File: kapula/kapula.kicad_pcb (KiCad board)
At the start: 4 copper layers, 50 x 59 mm, 156 parts, among them J1 Conn_02x10_Odd_Even, J12 U.FL, J13 U.FL, J3 U.FL, J4 Conn_ARM_JTAG_SWD_10, J5 U.FL, J9 U.FL, Q1 AO3401A, Q2 AO3401A, Q3 AO3400A, Q4 BSS84, Q5 AO3400A, Q6 AO3400A, T1 BW21S7511A01TF, T2 BW21S7511A01TF, T3 BW21S7511A01TF, T4 BW21S7511A01TF, U1 XC6206P332MR, U2 TP4054, U3 DW01+G, U5 EFR32FG14P233F256GM48-B, U6 XA213-G4J, X1 DSB221SDN, Y1 32768 Hz

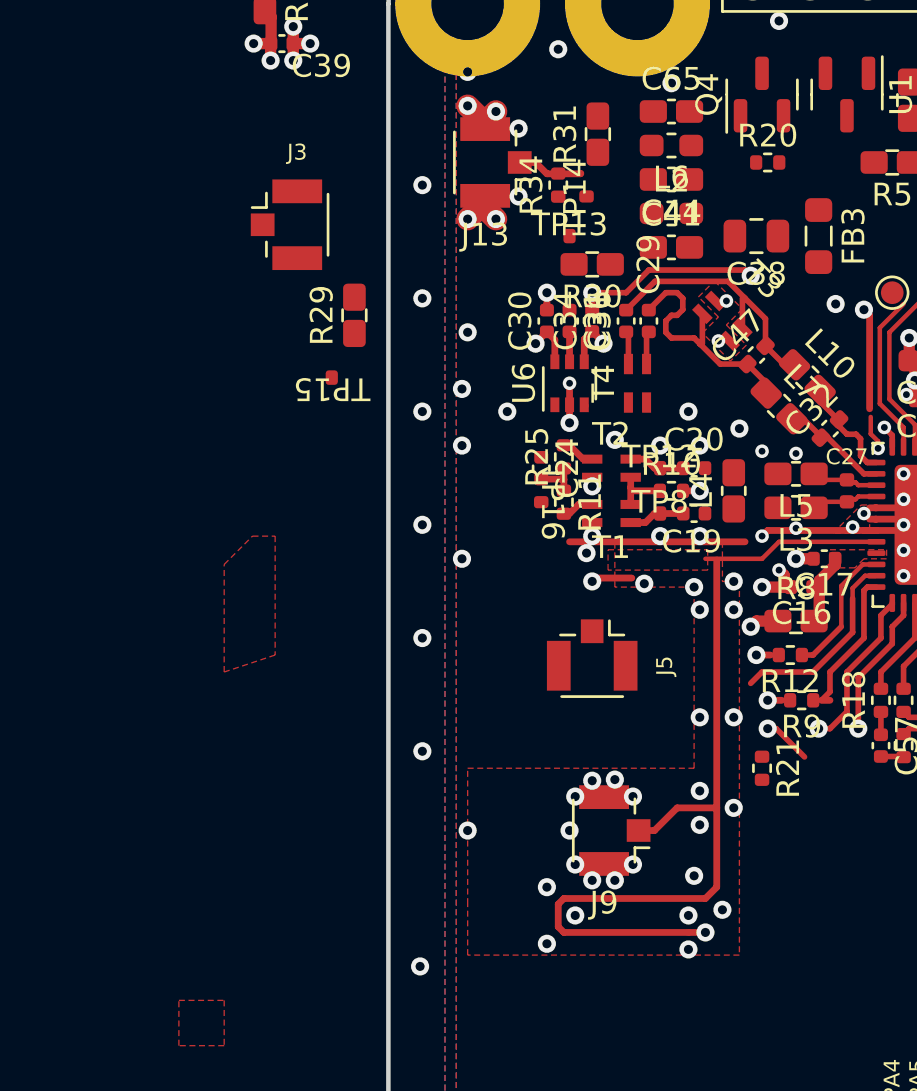
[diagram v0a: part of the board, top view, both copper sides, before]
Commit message: PCB: Organize RF layout
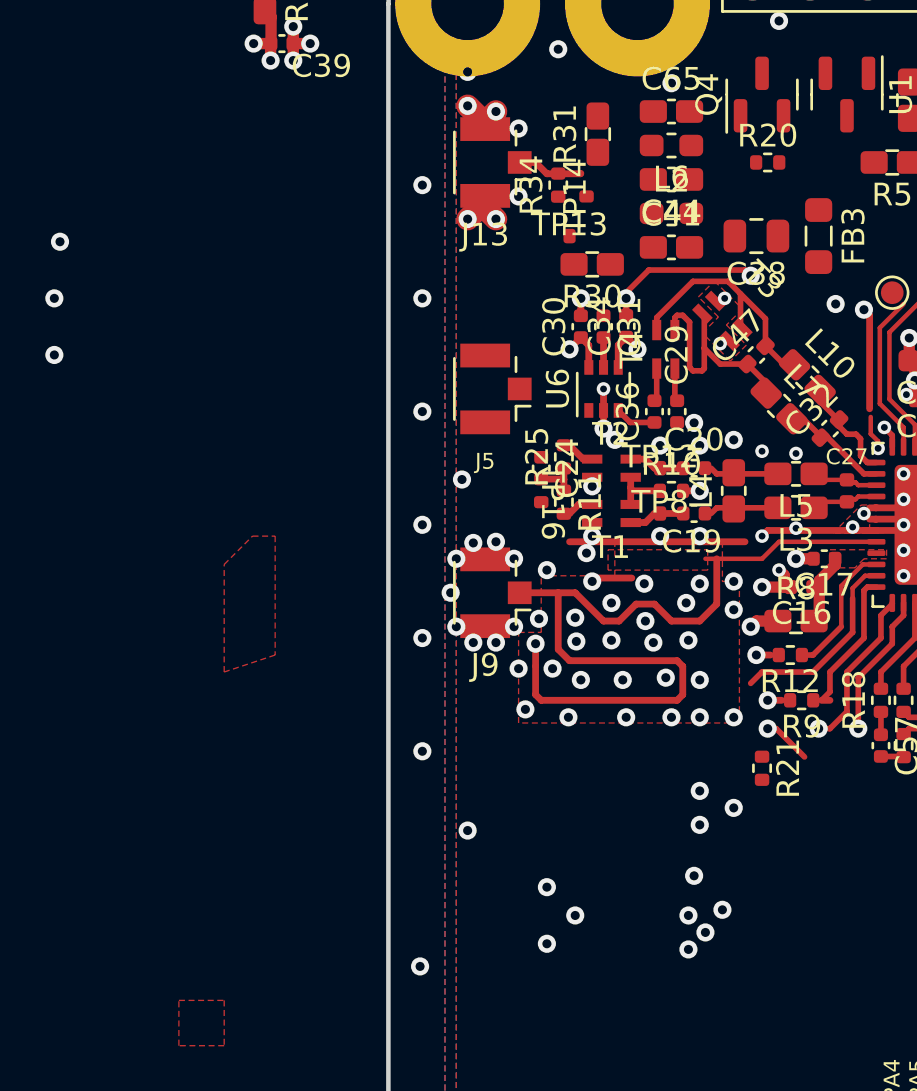
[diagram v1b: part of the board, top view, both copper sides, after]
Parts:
- removed J3: U.FL, Connector_Coaxial:U.FL_Hirose_U.FL-R-SMT-1_Vertical
- removed R29: 0, kapula:R_0402_to_0603_HandSolder
- removed TP15: ~, kapula:Pad_0402_1005Metric
- moved NT1 14.2 mm to (106.5, 89.8), turned to 90 degrees
- moved J5 12.5 mm to (104.8, 78.0), turned to 180 degrees
- moved J9 11.7 mm to (104.8, 87.0)
- moved C29 4.19 mm to (112.8, 79.0)
- moved C36 4.19 mm to (111.8, 79.0)
- moved T4 1.95 mm to (112.2, 76.2)
- moved C30 1.52 mm to (108.5, 75.2)
- moved C31 1.52 mm to (109.5, 75.2)
- moved C34 1.52 mm to (110.5, 75.2)
- moved U6 1.52 mm to (109.5, 78.0)
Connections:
- C29 pad 1: Net-(C29-Pad1) -> GND
- C36 pad 1: Net-(C36-Pad1) -> /RFSW_TX
- C47 pad 1: Net-(C29-Pad2) -> Net-(C47-Pad1)
- C47 pad 2: Net-(C36-Pad2) -> Net-(C47-Pad2)
- L10 pad 1: Net-(C36-Pad2) -> Net-(C47-Pad2)
- L7 pad 1: Net-(C29-Pad2) -> Net-(C47-Pad1)
- T3 pad 2: Net-(C36-Pad2) -> Net-(C47-Pad2)
- T3 pad 4: Net-(C29-Pad2) -> Net-(C47-Pad1)
- T4 pad 1: /RF_TX -> Net-(C36-Pad2)
- T4 pad 2: Net-(C36-Pad1) -> Net-(C47-Pad2)
- T4 pad 3: Net-(C29-Pad1) -> Net-(C47-Pad1)
- T4 pad 4: GND -> Net-(C29-Pad2)
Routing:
- net /TX_EN_SW: track 27.2 -> 3.86 mm
- net /RX_EN_SW: track 23.1 -> 2.82 mm, vias 3 -> 2
- net Net-(C47-Pad2): track 0.00 -> 11.4 mm
- net Net-(C47-Pad1): track 0.00 -> 10.7 mm
- net Net-(C36-Pad2): track 11.6 -> 1.46 mm
- net Net-(C29-Pad2): track 11.1 -> 1.46 mm
- net GND: track 91.1 -> 94.5 mm, vias 170 -> 190
- net Net-(C20-Pad2): track 0.00 -> 3.05 mm
- net Net-(C19-Pad2): track 0.00 -> 3.05 mm
- net /RF_2G4: track 40.1 -> 37.3 mm
- net /RFSW_TX: track 0.07 -> 1.89 mm
- net Net-(C36-Pad1): track 1.46 -> 0.00 mm
- net Net-(C29-Pad1): track 1.46 -> 0.00 mm

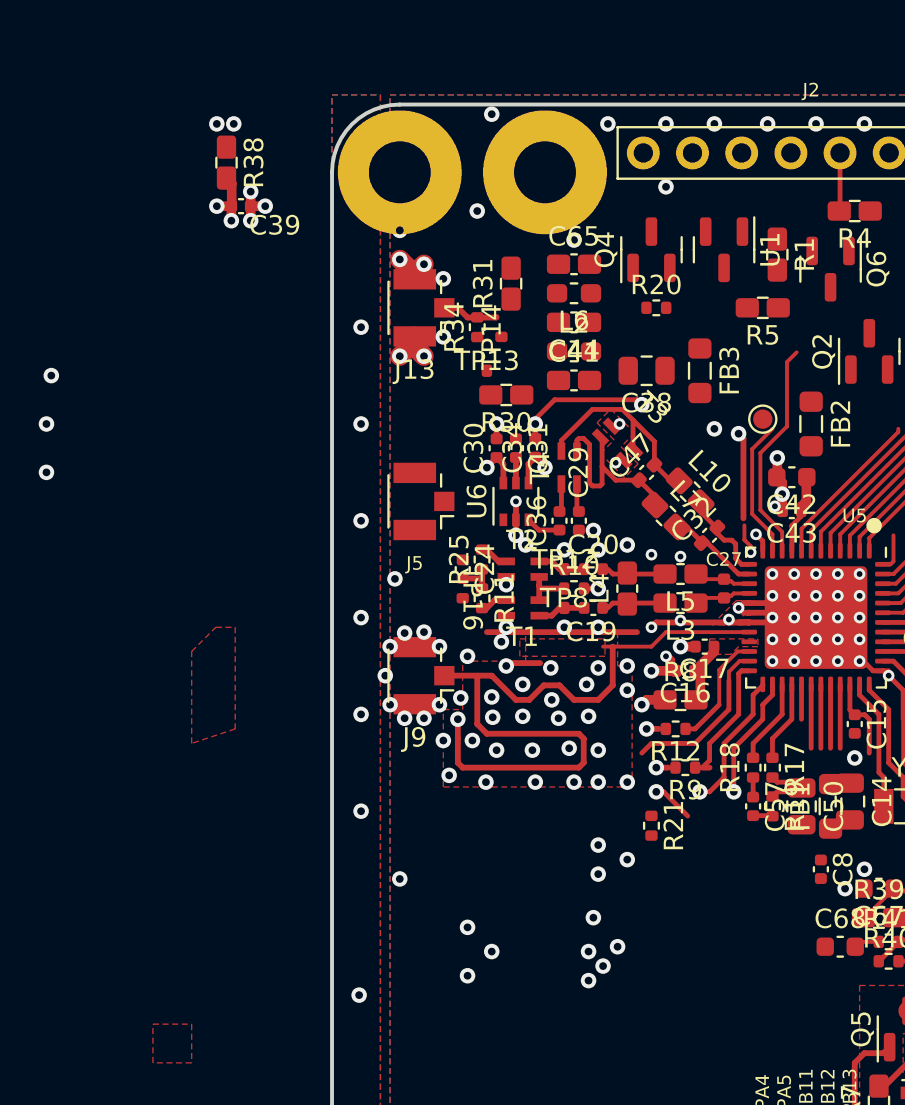
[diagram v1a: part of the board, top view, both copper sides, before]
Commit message: PCB: Layout more RF circuits
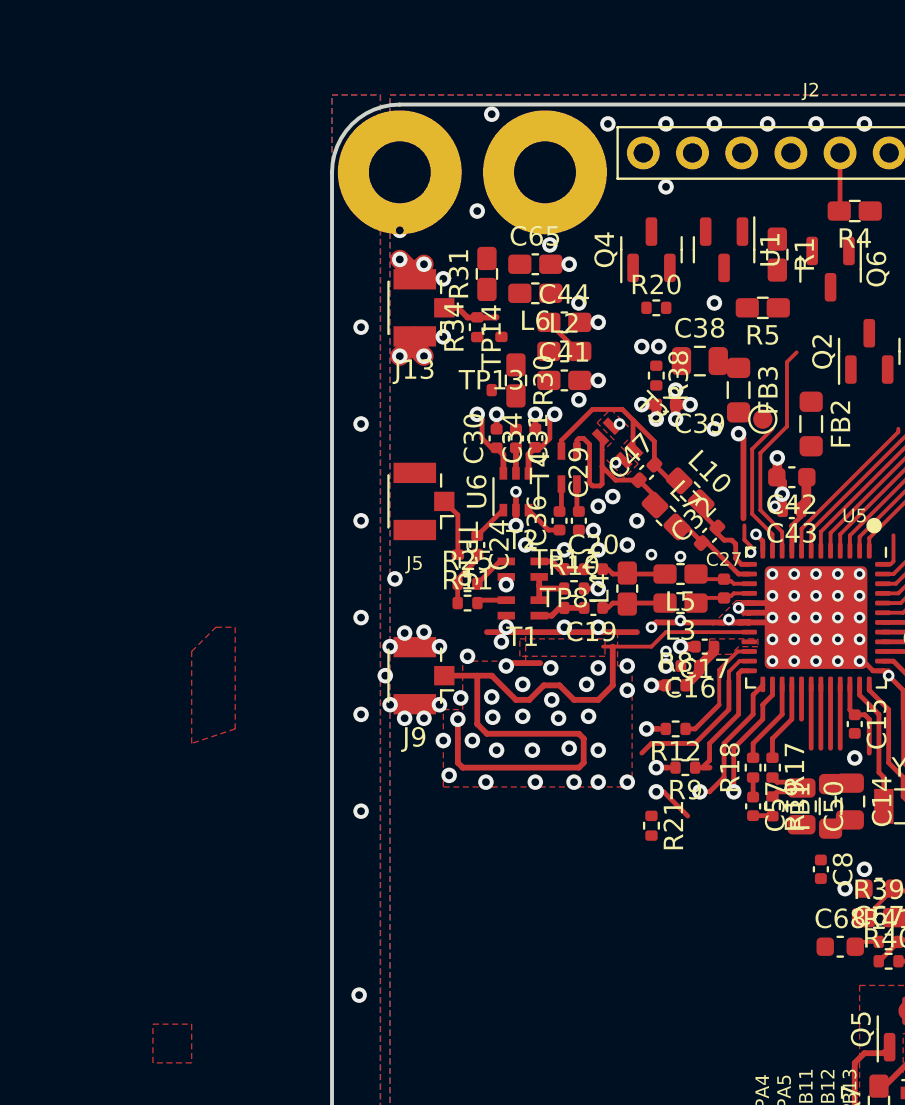
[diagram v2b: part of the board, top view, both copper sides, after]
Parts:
- C16: value 15p -> 220n
- C17: value 220n -> 15p
- L2, L6: value 18n -> 22n; footprint Inductor_SMD:L_0603_1608Metric_Pad1.05x0.95mm_HandSolder -> kapula:L_0402_to_0603_HandSolder
- R38, R8: footprint kapula:R_0402_to_0603_HandSolder -> Resistor_SMD:R_0402_1005Metric
- moved R38 24.8 mm to (116.8, 71.5)
- moved C39 24.2 mm to (117.2, 73.0)
- moved C38 2.80 mm to (119.0, 70.8), turned to 0 degrees
- moved TP16 2.26 mm to (106.5, 80.8)
- moved FB3 2.24 mm to (121.0, 72.2)
- moved C65 2.00 mm to (110.5, 65.8)
- moved L6 2.00 mm to (110.5, 67.2)
- moved C24 1.46 mm to (107.5, 80.2)
- moved R25 1.46 mm to (107.0, 82.2), turned to 0 degrees
- moved R31 1.35 mm to (108.0, 66.2)
- moved TP13 1.03 mm to (108.2, 72.2)
- moved R30 0.90 mm to (109.5, 71.8), turned to -90 degrees
- moved R11 0.79 mm to (107.0, 83.2), turned to 0 degrees
- moved R8 0.79 mm to (117.8, 87.5)
- moved C30 0.50 mm to (108.5, 74.8)
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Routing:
- net GND: track 94.5 -> 86.7 mm, vias 190 -> 183
- net /RFP_RX: track 0.00 -> 3.04 mm
- net Net-(C44-Pad1): track 0.00 -> 2.22 mm
- net /RFSW_RX: track 0.00 -> 1.90 mm
- net /RX_EN_SW: track 2.82 -> 4.39 mm
- net /PAVDD_SubG: track 3.09 -> 1.53 mm
- net /TX_EN_SW: track 3.86 -> 5.40 mm
- net /RF_RX: track 1.99 -> 2.68 mm
- added copper zone on F.Cu, net /PAVDD_2G4
- removed copper zone on F.Cu, net /PAVDD

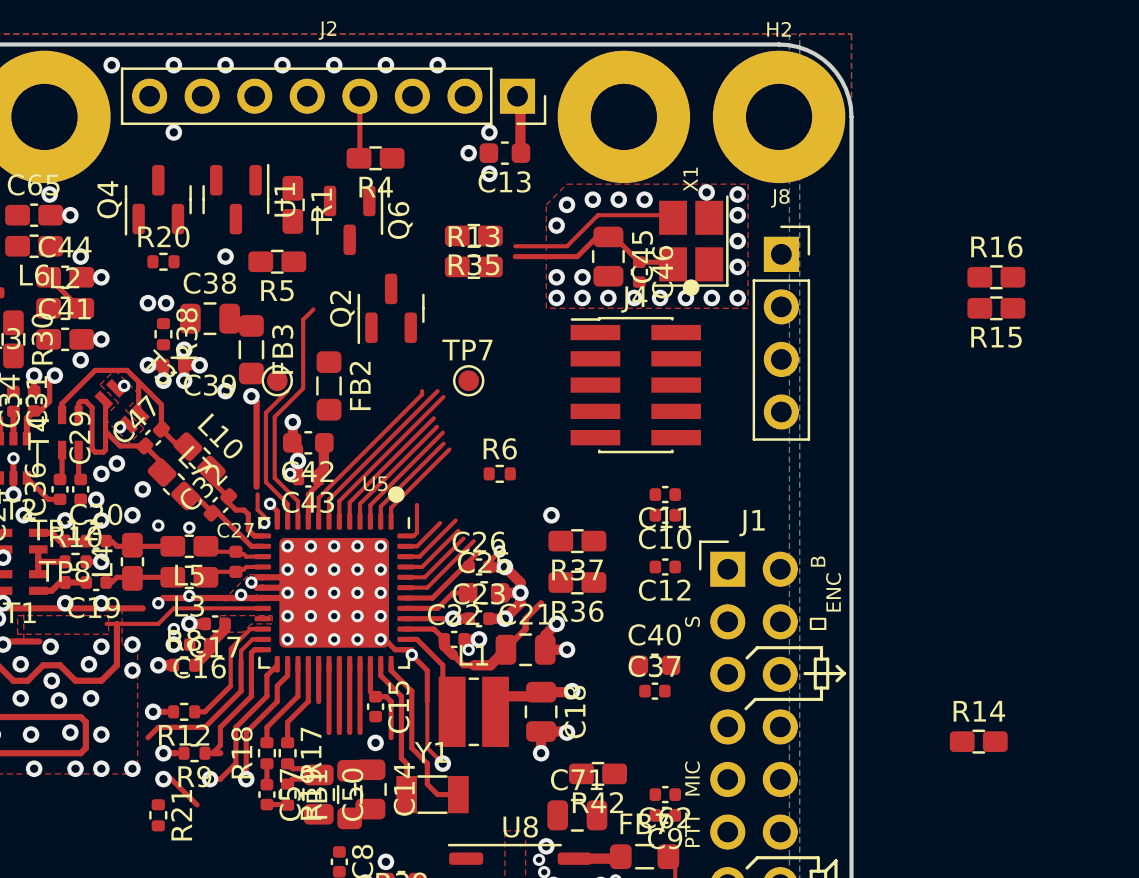
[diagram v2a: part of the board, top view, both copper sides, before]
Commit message: PCB: Route some display and connector lines
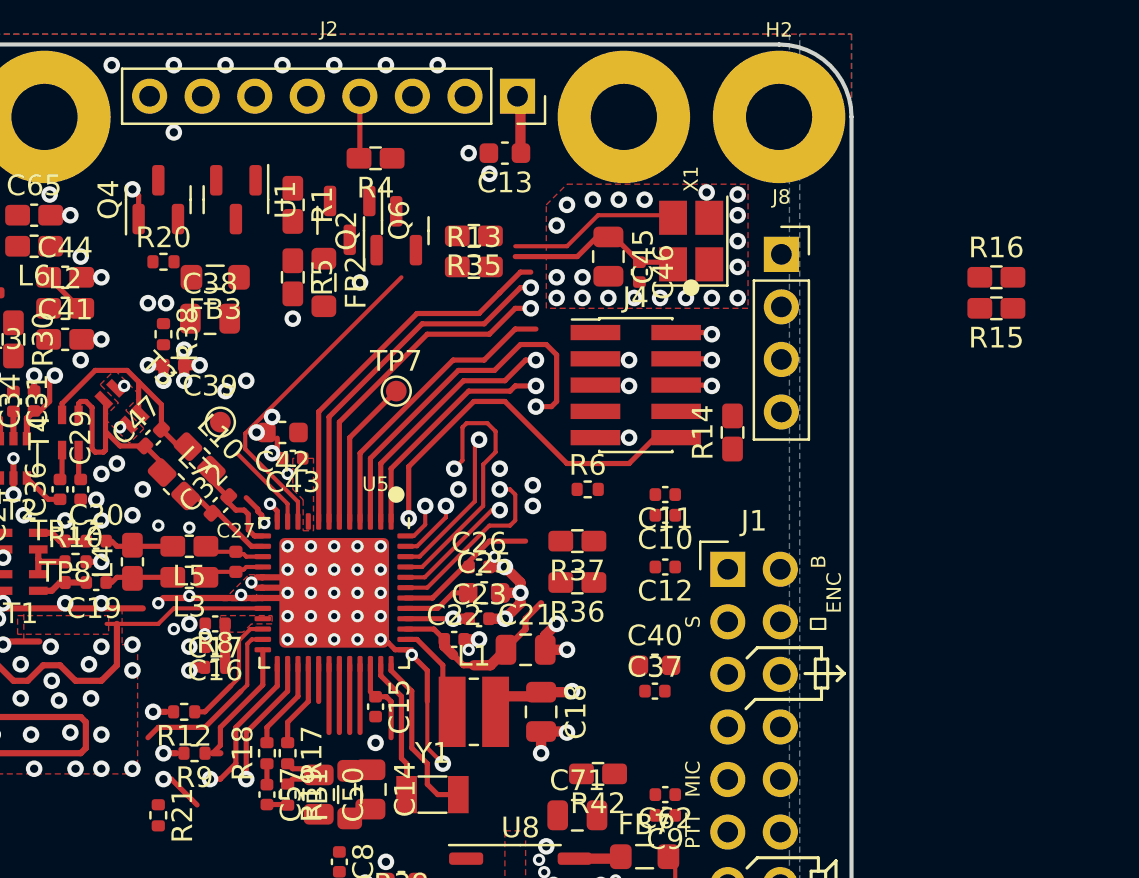
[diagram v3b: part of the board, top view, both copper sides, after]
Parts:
- moved R14 19.1 mm to (144.2, 76.2), turned to 90 degrees
- moved FB2 5.01 mm to (124.5, 69.0)
- moved R6 4.32 mm to (137.2, 79.0)
- moved FB3 3.91 mm to (119.2, 68.8), turned to 180 degrees
- moved Q2 3.76 mm to (128.0, 66.5)
- moved TP7 3.54 mm to (128.0, 74.2)
- moved TP11 3.40 mm to (119.5, 75.8)
- moved R8 1.50 mm to (119.2, 87.6)
- moved C42 1.35 mm to (122.5, 76.2)
- moved C43 1.25 mm to (123.0, 77.5)
- moved R5 1.06 mm to (123.0, 68.8), turned to -90 degrees
- moved C16 0.76 mm to (119.2, 86.6)
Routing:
- net /~{D_LED_EN}: track 2.14 -> 34.2 mm, vias 0 -> 2
- net /SWDIO_TMS: track 5.02 -> 28.8 mm, vias 0 -> 2
- net /SWO_TDO: track 5.75 -> 28.5 mm, vias 0 -> 2
- net /SWCLK_TCK: track 4.65 -> 27.0 mm, vias 0 -> 2
- net /D_CS: track 8.03 -> 28.8 mm, vias 0 -> 1
- net /RESET: track 5.97 -> 26.5 mm, vias 1 -> 2
- net /~{VDDS_EN}: track 1.96 -> 16.5 mm, vias 0 -> 2
- net /D_SCK: track 23.9 -> 38.3 mm, vias 0 -> 1
- net /D_AO: track 13.7 -> 27.6 mm, vias 0 -> 1
- net /RFVDD: track 12.3 -> 0.00 mm
- net /D_SDA: track 23.3 -> 34.1 mm, vias 0 -> 1
- net /Knob_S: track 8.37 -> 18.3 mm
- net /Knob_B: track 8.47 -> 17.4 mm, vias 0 -> 1
- net /Knob_A: track 8.10 -> 16.3 mm, vias 0 -> 1
- net /PF3_TDI: track 6.12 -> 14.3 mm
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- added copper zone on F.Cu, net /RFVDD

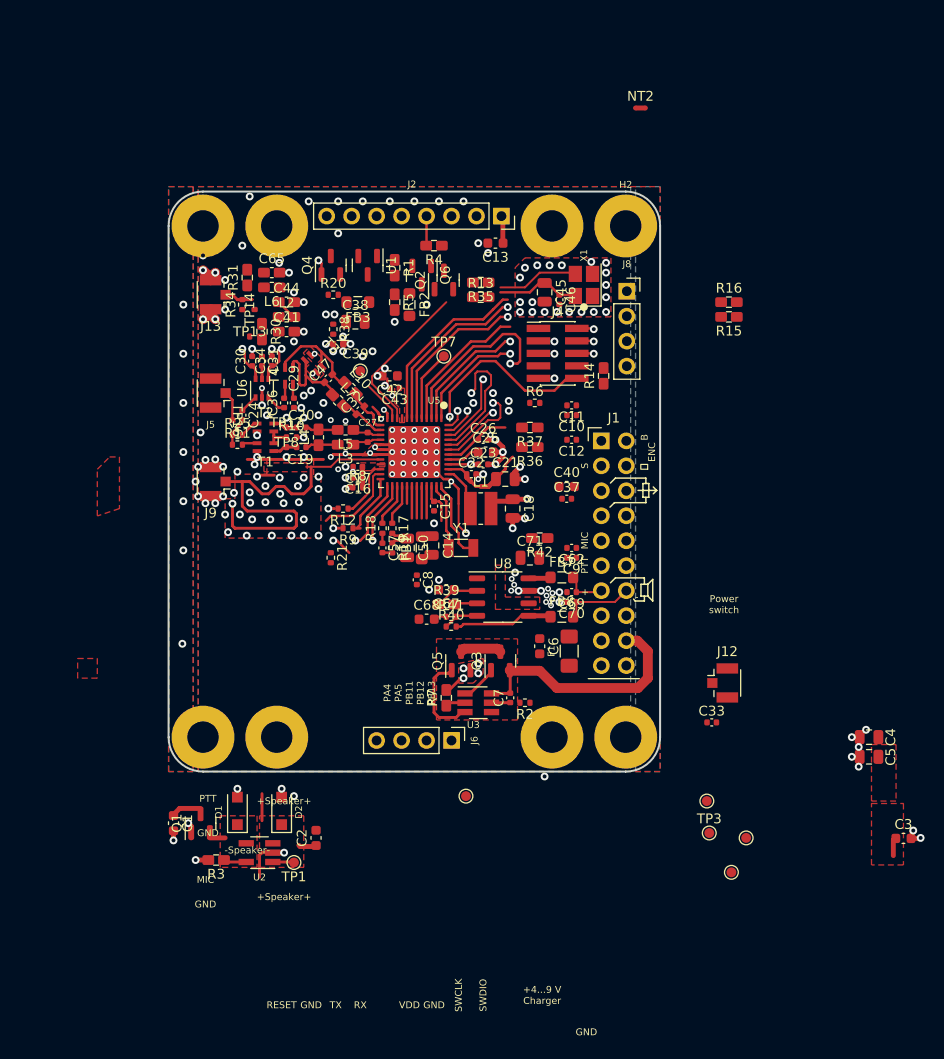
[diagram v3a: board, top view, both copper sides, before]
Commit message: PCB: Move components to make space for expansion header
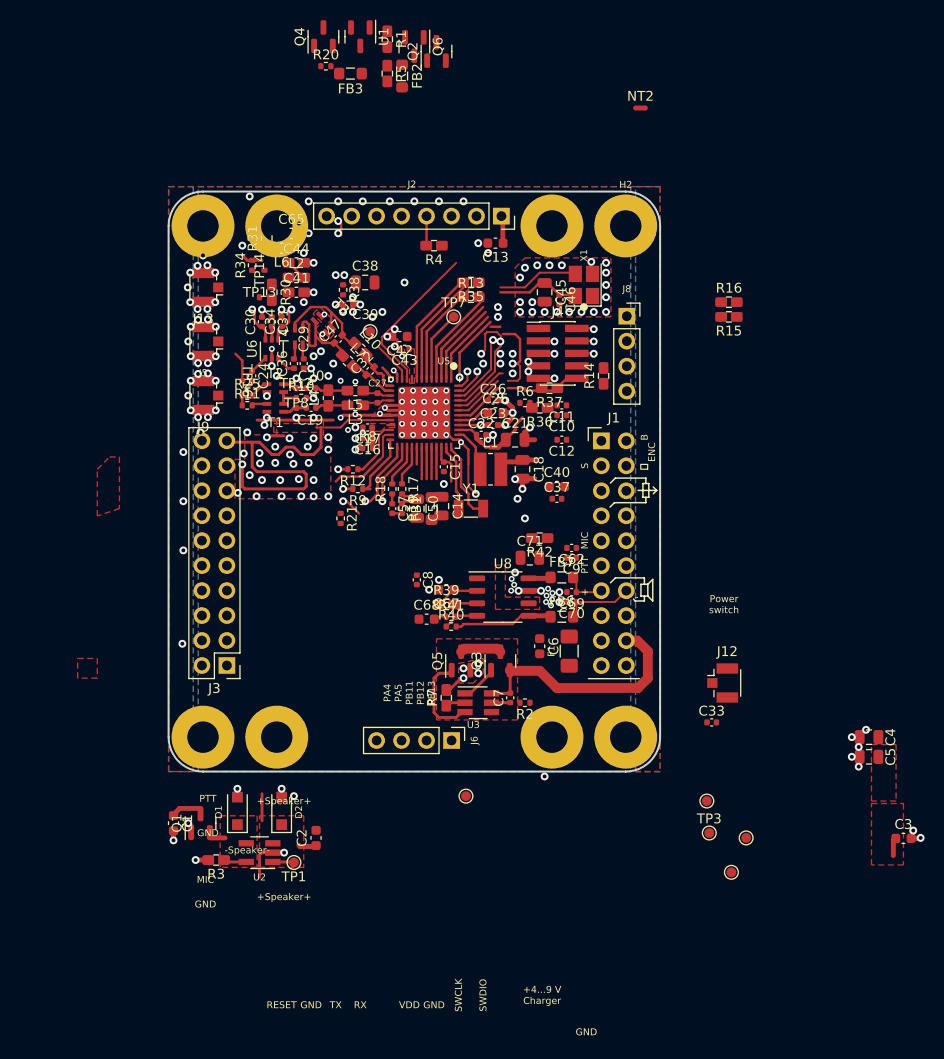
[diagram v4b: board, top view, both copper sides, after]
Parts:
- added J3: Conn_02x10_Odd_Even, Connector_PinHeader_2.54mm:PinHeader_2x10_P2.54mm_Vertical, F.Cu at (105.9, 105.7)
- moved FB2 23.3 mm to (123.8, 45.8)
- moved FB3 23.3 mm to (118.5, 45.5)
- moved Q2 23.3 mm to (127.2, 43.2)
- moved Q4 23.3 mm to (115.8, 41.8)
- moved Q6 23.3 mm to (125.0, 42.8)
- moved R1 23.3 mm to (122.2, 42.0)
- moved R20 23.3 mm to (116.0, 44.8)
- moved R5 23.3 mm to (122.2, 45.5)
- moved U1 23.3 mm to (119.5, 41.8)
- moved J9 8.78 mm to (104.0, 78.2)
- moved J5 5.30 mm to (104.0, 72.8)
- moved C65 4.47 mm to (112.5, 61.8)
- moved R31 4.47 mm to (110.0, 62.2)
- moved R37 4.47 mm to (138.8, 77.5)
- moved C14 4.12 mm to (127.8, 89.5)
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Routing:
- net /~{D_LED_EN}: track 34.2 -> 12.3 mm, vias 2 -> 1
- net GND: track 79.2 -> 93.2 mm, vias 190 -> 198
- net /D_CS: track 28.8 -> 16.2 mm
- net /D_SDA: track 34.1 -> 21.8 mm
- net /~{VDDS_EN}: track 16.5 -> 5.04 mm, vias 2 -> 1
- net /D_SCK: track 38.3 -> 28.8 mm
- net /D_AO: track 27.6 -> 19.2 mm
- net /Knob_S: track 18.3 -> 12.0 mm
- net /Knob_B: track 17.4 -> 11.4 mm, vias 1 -> 0
- net /RESET: track 26.5 -> 20.7 mm
- net /Knob_A: track 16.3 -> 10.8 mm
- net /PF3_TDI: track 14.3 -> 10.7 mm
- net /SWDIO_TMS: track 28.8 -> 25.4 mm
- net /SWCLK_TCK: track 27.0 -> 23.7 mm
- net /ANT_UFL: track 2.92 -> 2.22 mm
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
